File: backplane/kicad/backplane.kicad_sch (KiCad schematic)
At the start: 6 parts, among them J1 weactstm32h7xx, J2 pcie_98, J3 pcie_98, J4 pcie_98, J5 pcie_98, J6 pcie_98

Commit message: Work in progress. Backlane kicad.
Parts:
- removed J1: weactstm32h7xx, main_board:weact_stm32fh750, symbol main_board:weact_stm32h7xx
- added H1, H2, H3, H4, H5, H6: MountingHole, MountingHole:MountingHole_3.2mm_M3_Pad_Via, symbol Mechanical:MountingHole
- added J1: Conn_01x02_Pin, backplane:JST_XH_B2B-XH-AM_1x02_P2.50mm_Vertical, symbol Connector:Conn_01x02_Pin
- added J2: Conn_01x05_Pin, backplane:JST_XH_B5B-XH-AM_1x05_P2.50mm_Vertical, symbol Connector:Conn_01x05_Pin
- added S1, S7: pcie_98, backplane:pcie_98_socket, symbol backplane:pcie_98
- S2: renamed from J2; footprint main_board:pcie_98_socket -> backplane:pcie_98_socket; symbol main_board:pcie_98 -> backplane:pcie_98
- S3: renamed from J3; footprint main_board:pcie_98_socket -> backplane:pcie_98_socket; symbol main_board:pcie_98 -> backplane:pcie_98
- S4: renamed from J4; footprint main_board:pcie_98_socket -> backplane:pcie_98_socket; symbol main_board:pcie_98 -> backplane:pcie_98
- S5: renamed from J5; footprint main_board:pcie_98_socket -> backplane:pcie_98_socket; symbol main_board:pcie_98 -> backplane:pcie_98
- S6: renamed from J6; footprint main_board:pcie_98_socket -> backplane:pcie_98_socket; symbol main_board:pcie_98 -> backplane:pcie_98
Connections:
- net A1: now also S2.A1 (Pin_a1), S3.A1 (Pin_a1), S4.A1 (Pin_a1), S1.A1 (Pin_a1), S7.A1 (Pin_a1)
- net A10: now also S2.A10 (Pin_a10), S3.A10 (Pin_a10), S4.A10 (Pin_a10), S1.A10 (Pin_a10), S7.A10 (Pin_a10)
- net A11: now also S2.A11 (Pin_A11), S3.A11 (Pin_A11), S4.A11 (Pin_A11), S1.A11 (Pin_A11), S7.A11 (Pin_A11)
- net A2: now also S2.A2 (Pin_a2), S3.A2 (Pin_a2), S4.A2 (Pin_a2), S1.A2 (Pin_a2), S7.A2 (Pin_a2)
- net A3: now also S2.A3 (Pin_a3), S3.A3 (Pin_a3), S4.A3 (Pin_a3), S1.A3 (Pin_a3), S7.A3 (Pin_a3)
- net A4: now also S2.A4 (Pin_a4), S3.A4 (Pin_a4), S4.A4 (Pin_a4), S1.A4 (Pin_a4), S7.A4 (Pin_a4)
- net A5: now also S2.A5 (Pin_a5), S3.A5 (Pin_a5), S4.A5 (Pin_a5), S1.A5 (Pin_a5), S7.A5 (Pin_a5)
- net A6: now also S2.A6 (Pin_a6), S3.A6 (Pin_a6), S4.A6 (Pin_a6), S1.A6 (Pin_a6), S7.A6 (Pin_a6)
- net A7: now also S2.A7 (Pin_a7), S3.A7 (Pin_a7), S4.A7 (Pin_a7), S1.A7 (Pin_a7), S7.A7 (Pin_a7)
- net A8: now also S2.A8 (Pin_a8), S3.A8 (Pin_a8), S4.A8 (Pin_a8), S1.A8 (Pin_a8), S7.A8 (Pin_a8)
- net A9: now also S2.A9 (Pin_a9), S3.A9 (Pin_a9), S4.A9 (Pin_a9), S1.A9 (Pin_a9), S7.A9 (Pin_a9)
- net B1: now also S2.B1 (Pin_b1), S3.B1 (Pin_b1), S4.B1 (Pin_b1), S1.B1 (Pin_b1), S7.B1 (Pin_b1)
- net B10: now also S2.B10 (Pin_b10), S3.B10 (Pin_b10), S4.B10 (Pin_b10), S1.B10 (Pin_b10), S7.B10 (Pin_b10)
- net B11: now also S2.B11 (Pin_b11), S3.B11 (Pin_b11), S4.B11 (Pin_b11), S1.B11 (Pin_b11), S7.B11 (Pin_b11)
- net B2: now also S2.B2 (Pin_b2), S3.B2 (Pin_b2), S4.B2 (Pin_b2), S1.B2 (Pin_b2), S7.B2 (Pin_b2)
- net B3: now also S2.B3 (Pin_b3), S3.B3 (Pin_b3), S4.B3 (Pin_b3), S1.B3 (Pin_b3), S7.B3 (Pin_b3)
- net B4: now also S2.B4 (Pin_b4), S3.B4 (Pin_b4), S4.B4 (Pin_b4), S1.B4 (Pin_b4), S7.B4 (Pin_b4)
- net B5: now also S2.B5 (Pin_b5), S3.B5 (Pin_b5), S4.B5 (Pin_b5), S1.B5 (Pin_b5), S7.B5 (Pin_b5)
- net B6: now also S2.B6 (Pin_b6), S3.B6 (Pin_b6), S4.B6 (Pin_b6), S1.B6 (Pin_b6), S7.B6 (Pin_b6)
- net B7: now also S2.B7 (Pin_b7), S3.B7 (Pin_b7), S4.B7 (Pin_b7), S1.B7 (Pin_b7), S7.B7 (Pin_b7)
- net B8: now also S2.B8 (Pin_b8), S3.B8 (Pin_b8), S4.B8 (Pin_b8), S1.B8 (Pin_b8), S7.B8 (Pin_b8)
- net B9: now also S2.B9 (Pin_b9), S3.B9 (Pin_b9), S4.B9 (Pin_b9), S1.B9 (Pin_b9), S7.B9 (Pin_b9)
- net A12: now reaches S2.A12 (Pin_a12)
- net A12: now also S3.A12 (Pin_a12), S4.A12 (Pin_a12), S5.A12 (Pin_a12), S6.A12 (Pin_a12), S1.A12 (Pin_a12), S7.A12 (Pin_a12)
- net A13: now reaches S2.A13 (Pin_a13)
- net A13: now also S3.A13 (Pin_a13), S4.A13 (Pin_a13), S5.A13 (Pin_a13), S6.A13 (Pin_a13), S1.A13 (Pin_a13), S7.A13 (Pin_a13)
- net A14: now reaches S2.A14 (Pin_a14)
- net A14: now also S3.A14 (Pin_a14), S4.A14 (Pin_a14), S5.A14 (Pin_a14), S6.A14 (Pin_a14), S1.A14 (Pin_a14), S7.A14 (Pin_a14)
- net A15: now reaches S2.A15 (Pin_a15)
- net A15: now also S3.A15 (Pin_a15), S4.A15 (Pin_a15), S5.A15 (Pin_a15), S6.A15 (Pin_a15), S1.A15 (Pin_a15), S7.A15 (Pin_a15)
- net A16: now reaches S2.A16 (Pin_a16)
- net A16: now also S3.A16 (Pin_a16), S4.A16 (Pin_a16), S5.A16 (Pin_a16), S6.A16 (Pin_a16), S1.A16 (Pin_a16), S7.A16 (Pin_a16)
- net A17: now reaches S2.A17 (Pin_a17)
- net A17: now also S3.A17 (Pin_a17), S4.A17 (Pin_a17), S5.A17 (Pin_a17), S6.A17 (Pin_a17), S1.A17 (Pin_a17), S7.A17 (Pin_a17)
- net A18: now reaches S2.A18 (Pin_a18)
- net A18: now also S3.A18 (Pin_a18), S4.A18 (Pin_a18), S5.A18 (Pin_a18), S6.A18 (Pin_a18), S1.A18 (Pin_a18), S7.A18 (Pin_a18)
- net A19: now reaches S2.A19 (Pin_a19)
- net A19: now also S3.A19 (Pin_a19), S4.A19 (Pin_a19), S5.A19 (Pin_a19), S6.A19 (Pin_a19), S1.A19 (Pin_a19), S7.A19 (Pin_a19)
- net A21: now reaches S2.A21 (Pin_a21)
- net A21: now also S3.A21 (Pin_a21), S4.A21 (Pin_a21), S5.A21 (Pin_a21), S6.A21 (Pin_a21), S1.A21 (Pin_a21), S7.A21 (Pin_a21)
- net A22: now reaches S2.A22 (Pin_a22)
- net A22: now also S3.A22 (Pin_a22), S4.A22 (Pin_a22), S5.A22 (Pin_a22), S6.A22 (Pin_a22), S1.A22 (Pin_a22), S7.A22 (Pin_a22)
- net A23: now reaches S2.A23 (Pin_a23)
- net A23: now also S3.A23 (Pin_a23), S4.A23 (Pin_a23), S5.A23 (Pin_a23), S6.A23 (Pin_a23), S1.A23 (Pin_a23), S7.A23 (Pin_a23)
- net A24: now reaches S2.A24 (Pin_a24)
- net A24: now also S3.A24 (Pin_a24), S4.A24 (Pin_a24), S5.A24 (Pin_a24), S6.A24 (Pin_a24), S1.A24 (Pin_a24), S7.A24 (Pin_a24)
- net A25: now reaches S2.A25 (Pin_a25)
- net A25: now also S3.A25 (Pin_a25), S4.A25 (Pin_a25), S5.A25 (Pin_a25), S6.A25 (Pin_a25), S1.A25 (Pin_a25), S7.A25 (Pin_a25)
- net A26: now reaches S2.A26 (Pin_a26)
- net A26: now also S3.A26 (Pin_a26), S4.A26 (Pin_a26), S5.A26 (Pin_a26), S6.A26 (Pin_a26), S1.A26 (Pin_a26), S7.A26 (Pin_a26)
- net A27: now reaches S2.A27 (Pin_a27)
- net A27: now also S3.A27 (Pin_a27), S4.A27 (Pin_a27), S5.A27 (Pin_a27), S6.A27 (Pin_a27), S1.A27 (Pin_a27), S7.A27 (Pin_a27)
- net A28: now reaches S2.A28 (Pin_a28)
- net A28: now also S3.A28 (Pin_a28), S4.A28 (Pin_a28), S5.A28 (Pin_a28), S6.A28 (Pin_a28), S1.A28 (Pin_a28), S7.A28 (Pin_a28)
- net A29: now reaches S2.A29 (Pin_a29)
- net A29: now also S3.A29 (Pin_a29), S4.A29 (Pin_a29), S5.A29 (Pin_a29), S6.A29 (Pin_a29), S1.A29 (Pin_a29), S7.A29 (Pin_a29)
- net A30: now reaches S2.A30 (Pin_a30)
- net A30: now also S3.A30 (Pin_a30), S4.A30 (Pin_a30), S5.A30 (Pin_a30), S6.A30 (Pin_a30), S1.A30 (Pin_a30), S7.A30 (Pin_a30)
- net A31: now reaches S2.A31 (Pin_a31)
- net A31: now also S3.A31 (Pin_a31), S4.A31 (Pin_a31), S5.A31 (Pin_a31), S6.A31 (Pin_a31), S1.A31 (Pin_a31), S7.A31 (Pin_a31)
- net A32: now reaches S2.A32 (Pin_a32)
- net A32: now also S3.A32 (Pin_a32), S4.A32 (Pin_a32), S5.A32 (Pin_a32), S6.A32 (Pin_a32), S1.A32 (Pin_a32), S7.A32 (Pin_a32)
- net A33: now reaches S2.A33 (Pin_a33)
- net A33: now also S3.A33 (Pin_a33), S4.A33 (Pin_a33), S5.A33 (Pin_a33), S6.A33 (Pin_a33), S1.A33 (Pin_a33), S7.A33 (Pin_a33)
- net A34: now reaches S2.A34 (Pin_a34)
- net A34: now also S3.A34 (Pin_a34), S4.A34 (Pin_a34), S5.A34 (Pin_a34), S6.A34 (Pin_a34), S1.A34 (Pin_a34), S7.A34 (Pin_a34)
- net A35: now reaches S2.A35 (Pin_a35)
- net A35: now also S3.A35 (Pin_a35), S4.A35 (Pin_a35), S5.A35 (Pin_a35), S6.A35 (Pin_a35), S1.A35 (Pin_a35), S7.A35 (Pin_a35)
- net A36: now reaches S2.A36 (Pin_a36)
- net A36: now also S3.A36 (Pin_a36), S4.A36 (Pin_a36), S5.A36 (Pin_a36), S6.A36 (Pin_a36), S1.A36 (Pin_a36), S7.A36 (Pin_a36)
- net A37: now reaches S2.A37 (Pin_a37)
- net A37: now also S3.A37 (Pin_a37), S4.A37 (Pin_a37), S5.A37 (Pin_a37), S6.A37 (Pin_a37), S1.A37 (Pin_a37), S7.A37 (Pin_a37)
- net A38: now reaches S2.A38 (Pin_a38)
- net A38: now also S3.A38 (Pin_a38), S4.A38 (Pin_a38), S5.A38 (Pin_a38), S6.A38 (Pin_a38), S1.A38 (Pin_a38), S7.A38 (Pin_a38)
- net A39: now reaches S2.A39 (Pin_a39)
- net A39: now also S3.A39 (Pin_a39), S4.A39 (Pin_a39), S5.A39 (Pin_a39), S6.A39 (Pin_a39), S1.A39 (Pin_a39), S7.A39 (Pin_a39)
- net A40: now reaches S2.A40 (Pin_a40)
- net A40: now also S3.A40 (Pin_a40), S4.A40 (Pin_a40), S5.A40 (Pin_a40), S6.A40 (Pin_a40), S1.A40 (Pin_a40), S7.A40 (Pin_a40)
- net A41: now reaches S2.A41 (Pin_a41)
- net A41: now also S3.A41 (Pin_a41), S4.A41 (Pin_a41), S5.A41 (Pin_a41), S6.A41 (Pin_a41), S1.A41 (Pin_a41), S7.A41 (Pin_a41)
- net A42: now reaches S2.A42 (Pin_a42)
- net A42: now also S3.A42 (Pin_a42), S4.A42 (Pin_a42), S5.A42 (Pin_a42), S6.A42 (Pin_a42), S1.A42 (Pin_a42), S7.A42 (Pin_a42)
- net A43: now reaches S2.A43 (Pin_a43)
- net A43: now also S3.A43 (Pin_a43), S4.A43 (Pin_a43), S5.A43 (Pin_a43), S6.A43 (Pin_a43), S1.A43 (Pin_a43), S7.A43 (Pin_a43)
- net A44: now reaches S2.A44 (Pin_a44)
- net A44: now also S3.A44 (Pin_a44), S4.A44 (Pin_a44), S5.A44 (Pin_a44), S6.A44 (Pin_a44), S1.A44 (Pin_a44), S7.A44 (Pin_a44)
- net A45: now reaches S2.A45 (Pin_a45)
- net A45: now also S3.A45 (Pin_a45), S4.A45 (Pin_a45), S5.A45 (Pin_a45), S6.A45 (Pin_a45), S1.A45 (Pin_a45), S7.A45 (Pin_a45)
- net A46: now reaches S2.A46 (Pin_a46)
- net A46: now also S3.A46 (Pin_a46), S4.A46 (Pin_a46), S5.A46 (Pin_a46), S6.A46 (Pin_a46), S1.A46 (Pin_a46), S7.A46 (Pin_a46)
- net A47: now reaches S2.A47 (Pin_a47)
- net A47: now also S3.A47 (Pin_a47), S4.A47 (Pin_a47), S5.A47 (Pin_a47), S6.A47 (Pin_a47), S1.A47 (Pin_a47), S7.A47 (Pin_a47)
- net A48: now reaches S2.A48 (Pin_a48)
- net A48: now also S3.A48 (Pin_a48), S4.A48 (Pin_a48), S5.A48 (Pin_a48), S6.A48 (Pin_a48), S1.A48 (Pin_a48), S7.A48 (Pin_a48)
- net A49: now reaches S2.A49 (Pin_a49)
- net A49: now also S3.A49 (Pin_a49), S4.A49 (Pin_a49), S5.A49 (Pin_a49), S6.A49 (Pin_a49), S1.A49 (Pin_a49), S7.A49 (Pin_a49)
- net B12: now reaches S2.B12 (Pin_b12)
- net B12: now also S3.B12 (Pin_b12), S4.B12 (Pin_b12), S5.B12 (Pin_b12), S6.B12 (Pin_b12), S1.B12 (Pin_b12), S7.B12 (Pin_b12)
- net B13: now reaches S2.B13 (Pin_b13)
- net B13: now also S3.B13 (Pin_b13), S4.B13 (Pin_b13), S5.B13 (Pin_b13), S6.B13 (Pin_b13), S1.B13 (Pin_b13), S7.B13 (Pin_b13)
- net B14: now reaches S2.B14 (Pin_b14)
- net B14: now also S3.B14 (Pin_b14), S4.B14 (Pin_b14), S5.B14 (Pin_b14), S6.B14 (Pin_b14), S1.B14 (Pin_b14), S7.B14 (Pin_b14)
- net B15: now reaches S2.B15 (Pin_b15)
- net B15: now also S3.B15 (Pin_b15), S4.B15 (Pin_b15), S5.B15 (Pin_b15), S6.B15 (Pin_b15), S1.B15 (Pin_b15), S7.B15 (Pin_b15)
- net B16: now reaches S2.B16 (Pin_b16)
- net B16: now also S3.B16 (Pin_b16), S4.B16 (Pin_b16), S5.B16 (Pin_b16), S6.B16 (Pin_b16), S1.B16 (Pin_b16), S7.B16 (Pin_b16)
- net B17: now reaches S2.B17 (Pin_b17)
- net B17: now also S3.B17 (Pin_b17), S4.B17 (Pin_b17), S5.B17 (Pin_b17), S6.B17 (Pin_b17), S1.B17 (Pin_b17), S7.B17 (Pin_b17)
- net B18: now reaches S2.B18 (Pin_b18)
- net B18: now also S3.B18 (Pin_b18), S4.B18 (Pin_b18), S5.B18 (Pin_b18), S6.B18 (Pin_b18), S1.B18 (Pin_b18), S7.B18 (Pin_b18)
- net B19: now reaches S2.B19 (Pin_b19)
- net B19: now also S3.B19 (Pin_b19), S4.B19 (Pin_b19), S5.B19 (Pin_b19), S6.B19 (Pin_b19), S1.B19 (Pin_b19), S7.B19 (Pin_b19)
- net B20: now reaches S2.B20 (Pin_b20)
- net B20: now also S3.B20 (Pin_b20), S4.B20 (Pin_b20), S5.B20 (Pin_b20), S6.B20 (Pin_b20), S1.B20 (Pin_b20), S7.B20 (Pin_b20)
- net B21: now reaches S2.B21 (Pin_b21)
- net B21: now also S3.B21 (Pin_b21), S4.B21 (Pin_b21), S5.B21 (Pin_b21), S6.B21 (Pin_b21), S1.B21 (Pin_b21), S7.B21 (Pin_b21)
- net B22: now reaches S2.B22 (Pin_b22)
- net B22: now also S3.B22 (Pin_b22), S4.B22 (Pin_b22), S5.B22 (Pin_b22), S6.B22 (Pin_b22), S1.B22 (Pin_b22), S7.B22 (Pin_b22)
- net B23: now reaches S2.B23 (Pin_b23)
- net B23: now also S3.B23 (Pin_b23), S4.B23 (Pin_b23), S5.B23 (Pin_b23), S6.B23 (Pin_b23), S1.B23 (Pin_b23), S7.B23 (Pin_b23)
- net B24: now reaches S2.B24 (Pin_b24)
- net B24: now also S3.B24 (Pin_b24), S4.B24 (Pin_b24), S5.B24 (Pin_b24), S6.B24 (Pin_b24), S1.B24 (Pin_b24), S7.B24 (Pin_b24)
- net B25: now reaches S2.B25 (Pin_b25)
- net B25: now also S3.B25 (Pin_b25), S4.B25 (Pin_b25), S5.B25 (Pin_b25), S6.B25 (Pin_b25), S1.B25 (Pin_b25), S7.B25 (Pin_b25)
- net B26: now reaches S2.B26 (Pin_b26)
- net B26: now also S3.B26 (Pin_b26), S4.B26 (Pin_b26), S5.B26 (Pin_b26), S6.B26 (Pin_b26), S1.B26 (Pin_b26), S7.B26 (Pin_b26)
- net B27: now reaches S2.B27 (Pin_b27)
- net B27: now also S3.B27 (Pin_b27), S4.B27 (Pin_b27), S5.B27 (Pin_b27), S6.B27 (Pin_b27), S1.B27 (Pin_b27), S7.B27 (Pin_b27)
- net B28: now reaches S2.B28 (Pin_b28)
- net B28: now also S3.B28 (Pin_b28), S4.B28 (Pin_b28), S5.B28 (Pin_b28), S6.B28 (Pin_b28), S1.B28 (Pin_b28), S7.B28 (Pin_b28)
- net B29: now reaches S2.B29 (Pin_b29)
- net B29: now also S3.B29 (Pin_b29), S4.B29 (Pin_b29), S5.B29 (Pin_b29), S6.B29 (Pin_b29), S1.B29 (Pin_b29), S7.B29 (Pin_b29)
- net B30: now reaches S2.B30 (Pin_b30)
- net B30: now also S3.B30 (Pin_b30), S4.B30 (Pin_b30), S5.B30 (Pin_b30), S6.B30 (Pin_b30), S1.B30 (Pin_b30), S7.B30 (Pin_b30)
- net B31: now reaches S2.B31 (Pin_b31)
- net B31: now also S3.B31 (Pin_b31), S4.B31 (Pin_b31), S5.B31 (Pin_b31), S6.B31 (Pin_b31), S1.B31 (Pin_b31), S7.B31 (Pin_b31)
- net B32: now reaches S2.B32 (Pin_b32)
- net B32: now also S3.B32 (Pin_b32), S4.B32 (Pin_b32), S5.B32 (Pin_b32), S6.B32 (Pin_b32), S1.B32 (Pin_b32), S7.B32 (Pin_b32)
- net B33: now reaches S2.B33 (Pin_b33)
- net B33: now also S3.B33 (Pin_b33), S4.B33 (Pin_b33), S5.B33 (Pin_b33), S6.B33 (Pin_b33), S1.B33 (Pin_b33), S7.B33 (Pin_b33)
- net B34: now reaches S2.B34 (Pin_b34)
- net B34: now also S3.B34 (Pin_b34), S4.B34 (Pin_b34), S5.B34 (Pin_b34), S6.B34 (Pin_b34), S1.B34 (Pin_b34), S7.B34 (Pin_b34)
- net B35: now reaches S2.B35 (Pin_b35)
- net B35: now also S3.B35 (Pin_b35), S4.B35 (Pin_b35), S5.B35 (Pin_b35), S6.B35 (Pin_b35), S1.B35 (Pin_b35), S7.B35 (Pin_b35)
- net B36: now reaches S2.B36 (Pin_b36)
- net B36: now also S3.B36 (Pin_b36), S4.B36 (Pin_b36), S5.B36 (Pin_b36), S6.B36 (Pin_b36), S1.B36 (Pin_b36), S7.B36 (Pin_b36)
- net B37: now reaches S2.B37 (Pin_b37)
- net B37: now also S3.B37 (Pin_b37), S4.B37 (Pin_b37), S5.B37 (Pin_b37), S6.B37 (Pin_b37), S1.B37 (Pin_b37), S7.B37 (Pin_b37)
- net B38: now reaches S2.B38 (Pin_b38)
- net B38: now also S3.B38 (Pin_b38), S4.B38 (Pin_b38), S5.B38 (Pin_b38), S6.B38 (Pin_b38), S1.B38 (Pin_b38), S7.B38 (Pin_b38)
- net B39: now reaches S2.B39 (Pin_b39)
- net B39: now also S3.B39 (Pin_b39), S4.B39 (Pin_b39), S5.B39 (Pin_b39), S6.B39 (Pin_b39), S1.B39 (Pin_b39), S7.B39 (Pin_b39)
- net B40: now reaches S2.B40 (Pin_b40)
- net B40: now also S3.B40 (Pin_b40), S4.B40 (Pin_b40), S5.B40 (Pin_b40), S6.B40 (Pin_b40), S1.B40 (Pin_b40), S7.B40 (Pin_b40)
- net B41: now reaches S2.B41 (Pin_b41)
- net B41: now also S3.B41 (Pin_b41), S4.B41 (Pin_b41), S5.B41 (Pin_b41), S6.B41 (Pin_b41), S1.B41 (Pin_b41), S7.B41 (Pin_b41)
- net B42: now reaches S2.B42 (Pin_b42)
- net B42: now also S3.B42 (Pin_b42), S4.B42 (Pin_b42), S5.B42 (Pin_b42), S6.B42 (Pin_b42), S1.B42 (Pin_b42), S7.B42 (Pin_b42)
- net B43: now reaches S2.B43 (Pin_b43)
- net B43: now also S3.B43 (Pin_b43), S4.B43 (Pin_b43), S5.B43 (Pin_b43), S6.B43 (Pin_b43), S1.B43 (Pin_b43), S7.B43 (Pin_b43)
- net B44: now reaches S2.B44 (Pin_b44)
- net B44: now also S3.B44 (Pin_b44), S4.B44 (Pin_b44), S5.B44 (Pin_b44), S6.B44 (Pin_b44), S1.B44 (Pin_b44), S7.B44 (Pin_b44)
- net B45: now reaches S2.B45 (Pin_b45)
- net B45: now also S3.B45 (Pin_b45), S4.B45 (Pin_b45), S5.B45 (Pin_b45), S6.B45 (Pin_b45), S1.B45 (Pin_b45), S7.B45 (Pin_b45)
- net B46: now reaches S2.B46 (Pin_46)
- net B46: now also S3.B46 (Pin_46), S4.B46 (Pin_46), S5.B46 (Pin_46), S6.B46 (Pin_46), S1.B46 (Pin_46), S7.B46 (Pin_46)
- net B47: now reaches S2.B47 (Pin_b47)
- net B47: now also S3.B47 (Pin_b47), S4.B47 (Pin_b47), S5.B47 (Pin_b47), S6.B47 (Pin_b47), S1.B47 (Pin_b47), S7.B47 (Pin_b47)
- net B48: now reaches S2.B48 (Pin_b48)
- net B48: now also S3.B48 (Pin_b48), S4.B48 (Pin_b48), S5.B48 (Pin_b48), S6.B48 (Pin_b48), S1.B48 (Pin_b48), S7.B48 (Pin_b48)
- net B49: now reaches S2.B49 (Pin_b49)
- net B49: now also S3.B49 (Pin_b49), S4.B49 (Pin_b49), S5.B49 (Pin_b49), S6.B49 (Pin_b49), S1.B49 (Pin_b49), S7.B49 (Pin_b49)
- net A20: now reaches S2.a20 (Pin_a20)
- net A20: now also S3.a20 (Pin_a20), S4.a20 (Pin_a20), S5.a20 (Pin_a20), S6.a20 (Pin_a20), S1.A20 (Pin_a20), S7.a20 (Pin_a20)
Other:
- note added: "TODO: Add marking of slot pin numbering."
- note added: "TODO: Add silkscreen marking for power polarity and voltage (?)"
- note added: "TODO: Add silkscreen text/image with board name, version, etc."
- note added: "TODO: Assign ground pin(s), Verify PCIE connectors pinout and footprint. See 609-2031-ND"
- note added: "TODO: Assign ground pin(s), connect together and create ground pour if possible."
- note added: "TODO: Clean DRC"
- note added: "TODO: Clean ERC"
- note added: "TODO: Round corners"
- note added: "TODO: Wire the two auxilary connectors"
- note removed: "TODO: 1A 5v supply to boards"
- note removed: "TODO: Add bypass capacitors"
- note removed: "TODO: Clear silkscreen text for all the signals."
- note removed: "TODO: Power supply input"
- note removed: "TODO: Serial port for debugging."
- note removed: "TODO: ability to cut traces"
- note removed: "TODO: clarify orientation of inserting the weact"
- note removed: "TODO: mounting holes"
- title: (none) -> Backplane board
- moved on the sheet: S2, S3, S4, S5, S6

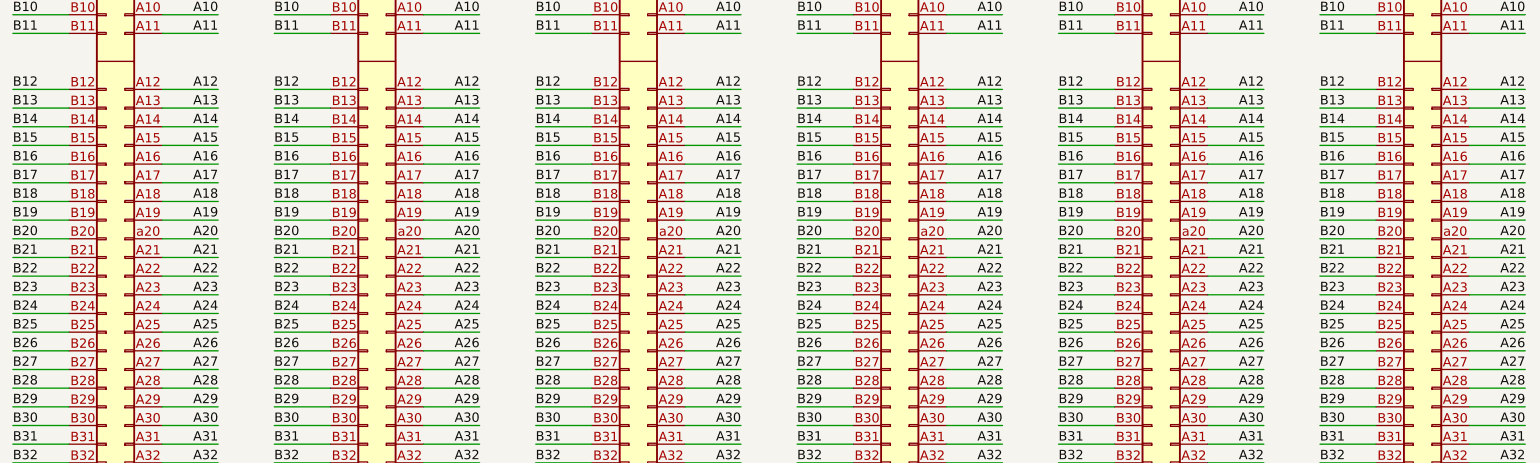
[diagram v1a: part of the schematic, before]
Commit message: Performed sample bus routing.
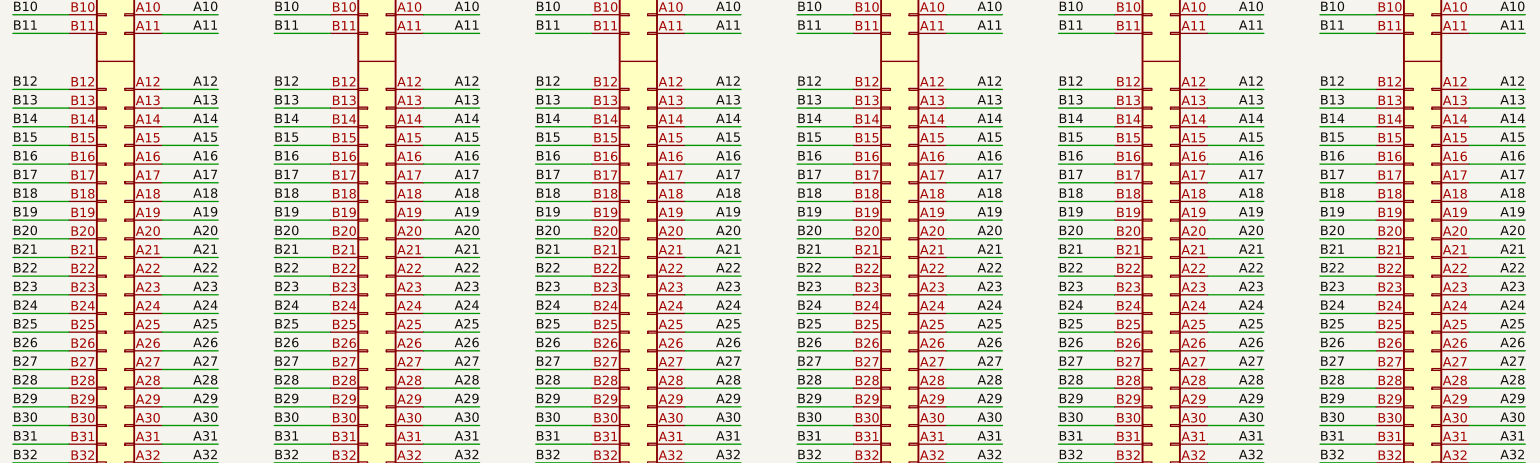
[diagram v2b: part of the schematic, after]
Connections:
- net A20: now also S2.A20 (Pin_a20), S3.A20 (Pin_a20), S4.A20 (Pin_a20), S5.A20 (Pin_a20), S6.A20 (Pin_a20), S7.A20 (Pin_a20); no longer S2.a20 (Pin_a20), S3.a20 (Pin_a20), S4.a20 (Pin_a20), S5.a20 (Pin_a20), S6.a20 (Pin_a20), S7.a20 (Pin_a20)

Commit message: outed all the network of the backplan.
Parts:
- J1: symbol Connector:Conn_01x02_Pin -> Connector_Generic:Conn_01x02
- J2: symbol Connector:Conn_01x05_Pin -> Connector_Generic:Conn_01x05
- S1, S2, S3, S4, S5, S6, S7: symbol backplane:pcie_98 -> backplane:pcie_98_socket
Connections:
- no-connect marks 0 -> 7
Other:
- note removed: "TODO: Add silkscreen marking for power polarity and voltage (?)"
- note removed: "TODO: Assign ground pin(s), Verify PCIE connectors pinout and footprint. See 609-2031-ND"
- note removed: "TODO: Clean DRC"
- note removed: "TODO: Clean ERC"
- note removed: "TODO: Round corners"
- note removed: "TODO: Wire the two auxilary connectors"
- moved on the sheet: S1, S2, S3, S4, S5, S6, S7

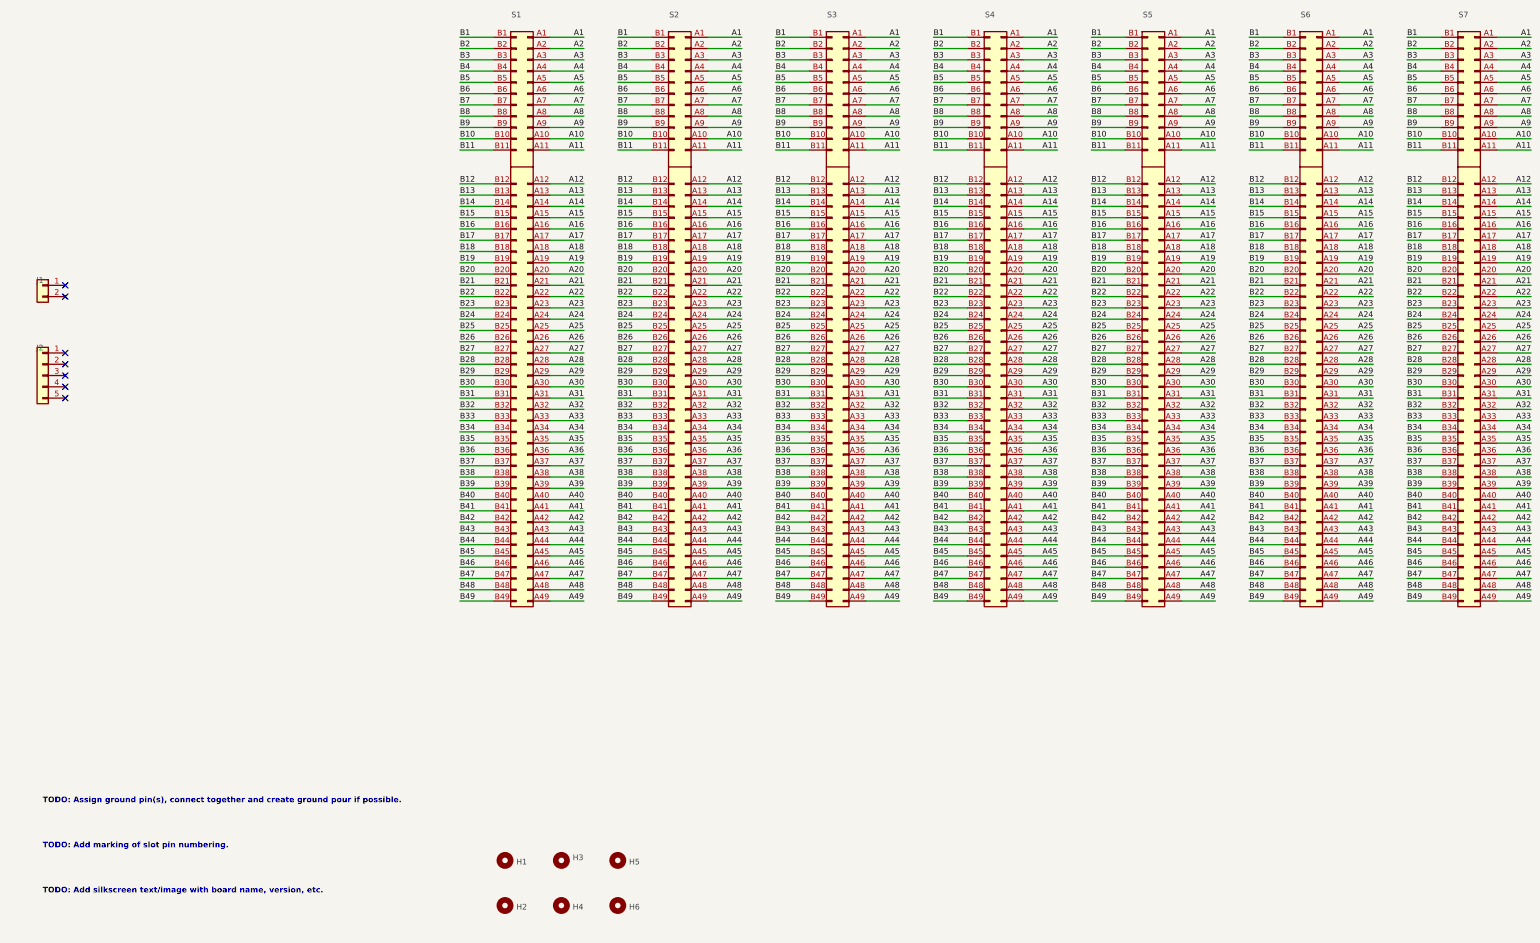
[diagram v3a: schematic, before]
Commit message: Completed the routing of the backplane.
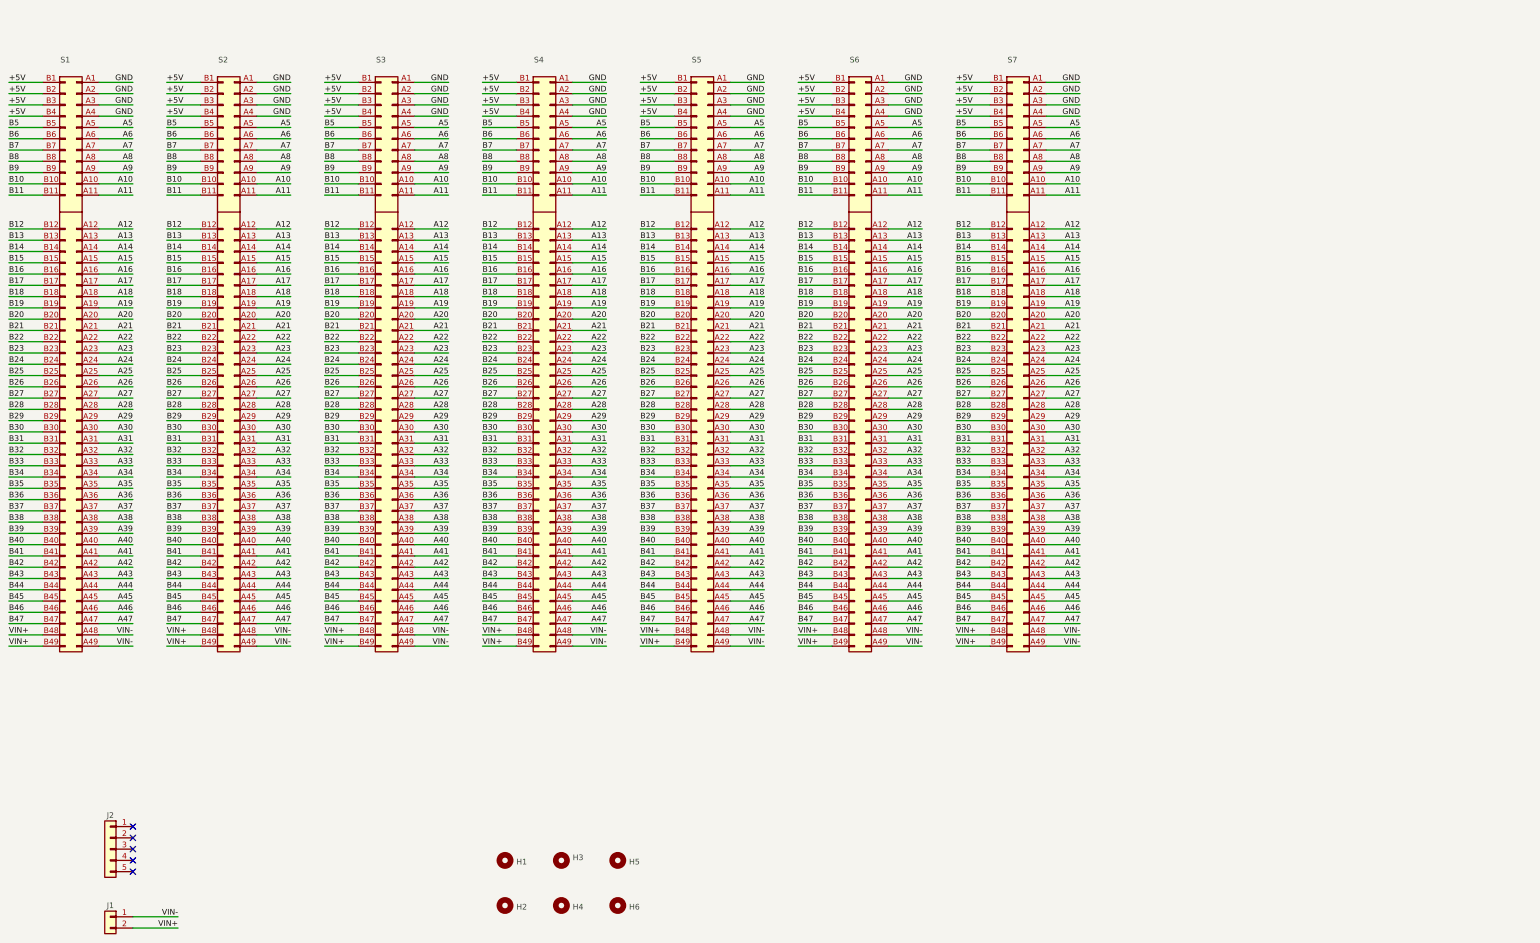
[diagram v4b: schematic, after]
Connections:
- net A2 is gone; now on net GND: S1.A2 (Pin_a2), S2.A2 (Pin_a2), S3.A2 (Pin_a2), S4.A2 (Pin_a2), S5.A2 (Pin_a2), S6.A2 (Pin_a2), S7.A2 (Pin_a2)
- net A3 is gone; now on net GND: S1.A3 (Pin_a3), S2.A3 (Pin_a3), S3.A3 (Pin_a3), S4.A3 (Pin_a3), S5.A3 (Pin_a3), S6.A3 (Pin_a3), S7.A3 (Pin_a3)
- net A4 is gone; now on net GND: S1.A4 (Pin_a4), S2.A4 (Pin_a4), S3.A4 (Pin_a4), S4.A4 (Pin_a4), S5.A4 (Pin_a4), S6.A4 (Pin_a4), S7.A4 (Pin_a4)
- net A48 is gone; now on net VIN-: S1.A48 (Pin_a48), S2.A48 (Pin_a48), S3.A48 (Pin_a48), S4.A48 (Pin_a48), S5.A48 (Pin_a48), S6.A48 (Pin_a48), S7.A48 (Pin_a48)
- net A49 is gone; now on net VIN-: S1.A49 (Pin_a49), S2.A49 (Pin_a49), S3.A49 (Pin_a49), S4.A49 (Pin_a49), S5.A49 (Pin_a49), S6.A49 (Pin_a49), S7.A49 (Pin_a49)
- net B2 is gone; now on net +5V: S1.B2 (Pin_b2), S2.B2 (Pin_b2), S3.B2 (Pin_b2), S4.B2 (Pin_b2), S5.B2 (Pin_b2), S6.B2 (Pin_b2), S7.B2 (Pin_b2)
- net B3 is gone; now on net +5V: S1.B3 (Pin_b3), S2.B3 (Pin_b3), S3.B3 (Pin_b3), S4.B3 (Pin_b3), S5.B3 (Pin_b3), S6.B3 (Pin_b3), S7.B3 (Pin_b3)
- net B4 is gone; now on net +5V: S1.B4 (Pin_b4), S2.B4 (Pin_b4), S3.B4 (Pin_b4), S4.B4 (Pin_b4), S5.B4 (Pin_b4), S6.B4 (Pin_b4), S7.B4 (Pin_b4)
- net B48 is gone; now on net VIN+: S1.B48 (Pin_b48), S2.B48 (Pin_b48), S3.B48 (Pin_b48), S4.B48 (Pin_b48), S5.B48 (Pin_b48), S6.B48 (Pin_b48), S7.B48 (Pin_b48)
- net B49 is gone; now on net VIN+: S1.B49 (Pin_b49), S2.B49 (Pin_b49), S3.B49 (Pin_b49), S4.B49 (Pin_b49), S5.B49 (Pin_b49), S6.B49 (Pin_b49), S7.B49 (Pin_b49)
- net VIN-: now reaches J1.1 (Pin_1)
- net VIN+: now reaches J1.2 (Pin_2)
- net A1 renamed GND
- net B1 renamed +5V
- no-connect marks 7 -> 5
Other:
- note removed: "TODO: Add marking of slot pin numbering."
- note removed: "TODO: Add silkscreen text/image with board name, version, etc."
- note removed: "TODO: Assign ground pin(s), connect together and create ground pour if possible."
- moved on the sheet: J1, J2, S1, S2, S3, S4, S5, S6, S7

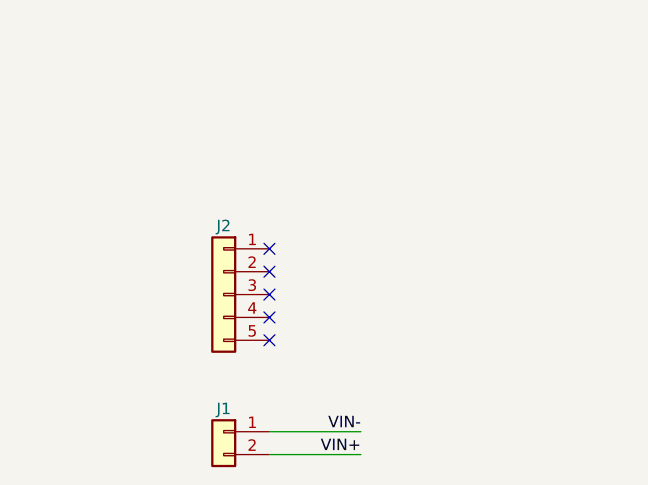
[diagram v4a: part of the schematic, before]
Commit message: Removed the backplane 5pins connector.
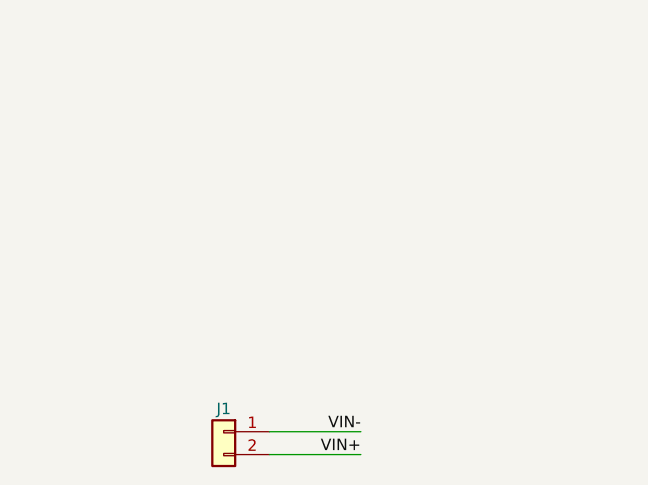
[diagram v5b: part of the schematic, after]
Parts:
- removed J2: Conn_01x05_Pin, backplane:JST_XH_B5B-XH-AM_1x05_P2.50mm_Vertical, symbol Connector_Generic:Conn_01x05
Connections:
- no-connect marks 5 -> 0
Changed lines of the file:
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@@
     (rev "0.1")
   )
-  (no_connect (at 78.74 233.68))
-  (no_connect (at 78.74 231.14))
-  (no_connect (at 78.74 228.6))
-  (no_connect (at 78.74 226.06))
-  (no_connect (at 78.74 236.22))
   (wire (pts (xy 142.24 71.12) (xy 149.86 71.12))
     (stroke (width 0) (type default))
@@
         )
       )
-    )
-  )
-  (symbol (lib_id "Connector_Generic:Conn_01x05") (at 73.66 231.14 0) (mirror y) (unit 1)
-    (in_bom yes) (on_board yes) (dnp no)
-    (property "Reference" "J2" (at 73.66 223.52 0)
-      (effects (font (size 1.27 1.27)))
-    )
-    (property "Value" "Conn_01x05_Pin" (at 73.025 224.8949 0)
-      (effects (font (size 1.27 1.27)) hide)
-    )
-    (property "Footprint" "backplane:JST_XH_B5B-XH-AM_1x05_P2.50mm_Vertical" (at 73.66 231.14 0)
-      (effects (font (size 1.27 1.27)) hide)
-    )
-    (property "Datasheet" "~" (at 73.66 231.14 0)
-      (effects (font (size 1.27 1.27)) hide)
-    )
-    (pin "1")
-    (pin "2")
-    (pin "3")
-    (pin "4")
-    (pin "5")
-    (instances
-      (project "backplane"
-        (path "/0dcd9c8c-bd5a-437f-856e-101fb6cf8b66"
-          (reference "J2") (unit 1)
-        )
-      )
